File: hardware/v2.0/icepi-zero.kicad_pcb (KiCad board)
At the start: 4 copper layers, 65 x 30 mm, 193 parts, among them IC1 IS42S16160J-6BLI, IC2 LTC2256CUJ-12#PBF, J1 Conn_02x20_Counter_Clockwise, J2 GPDI_C_1.3, J3 USB_C_Receptacle_USB2.0_14P, J4 USB_C_Receptacle_USB2.0_14P, J5 USB_C_Receptacle_USB2.0_14P, J6 Micro_SD_Card_Det2, J7 RSP-122811-01, SW1 SW_Push, SW2 SW_Push, U1 ECP5U-25F-CABGA256, U10 TPD2EUSB30A, U11 LT1993CUD-2_PBF, U12 W25Q128JVS, U2 LTC3407AEDD-2_PBF, U3 TLV62569DBV, U4 LP5912-1.8DRV, U5 TPD2EUSB30A, U6 PCA9306DC1, U7 TPD2EUSB30A, U8 TPD2EUSB30A, U9 FT231XQ, Y1 SG-8018CG 50.000000MHz, Y2 SG-8018CG 50.000000MHz

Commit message: DRC almost pass
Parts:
- added C74: 1u, Capacitor_SMD:C_0402_1005Metric, B.Cu at (170.4, 107.3)
- added R5: 1k, Resistor_SMD:R_0402_1005Metric, B.Cu at (169.5, 107.3)
- moved R52 0.78 mm to (169.6, 105.0), turned to 0 degrees
- moved C64 0.17 mm to (168.3, 107.3)
- moved C69 0.07 mm to (171.3, 106.6)
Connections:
- R52 pad 1: /ADC/VOCM -> Net-(IC2-VCM)
- R52 pad 2: Net-(IC2-VCM) -> /ADC/VOCM
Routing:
- net /ADC/SENSE: track 23.9 -> 26.7 mm
- net +1V8: track 29.6 -> 31.1 mm
- net Net-(IC2-VCM): track 4.72 -> 3.60 mm
- net /ADC/VOCM: track 6.82 -> 7.79 mm
- net GND: vias 100 -> 98
- net /ADC/CLKOUT-: vias 0 -> 2

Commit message: ADC SPI SDO
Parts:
- moved LOGO1 0.28 mm to (177.0, 110.3)
- moved R1 0.14 mm to (161.2, 112.0)
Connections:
- IC2 pad 16: unconnected-(IC2-SDO-Pad16) -> /ADC/SDO
- U1 pad C12: unconnected-(U1J-PT56B/--PadC12) -> /ADC/~{CS}
- U1 pad D13: /ADC/~{CS} -> /ADC/SDO
- U1 pad E12: /ADC/SDI -> /ADC/SENSE
- U1 pad E13: /ADC/SENSE -> /ADC/SDI
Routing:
- net /ADC/SDO: track 0.00 -> 34.8 mm, vias 0 -> 3
- net /ADC/~{CS}: track 30.2 -> 28.7 mm
- net +3V3: track 126.2 -> 127.3 mm
- net /ADC/SDI: track 34.2 -> 35.2 mm
- net /ADC/SENSE: track 26.7 -> 25.9 mm
- net /ADC/SCK: track 30.9 -> 30.2 mm

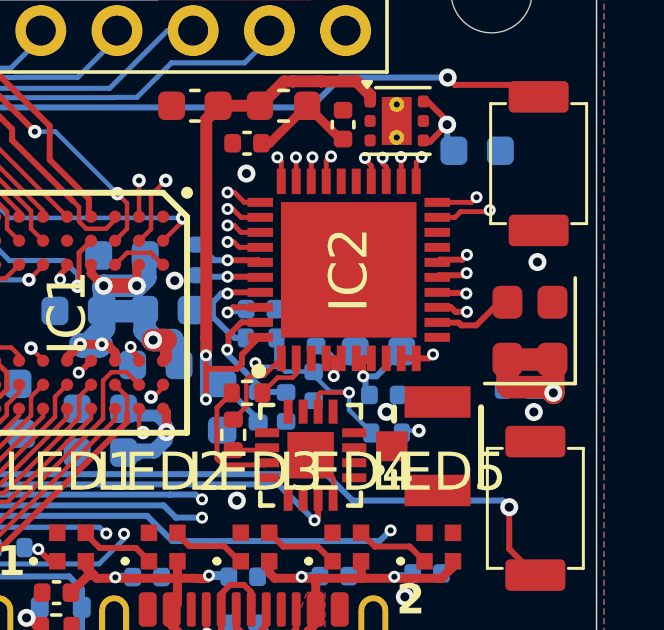
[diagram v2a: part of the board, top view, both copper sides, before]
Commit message: ADC SPI SDO pull up
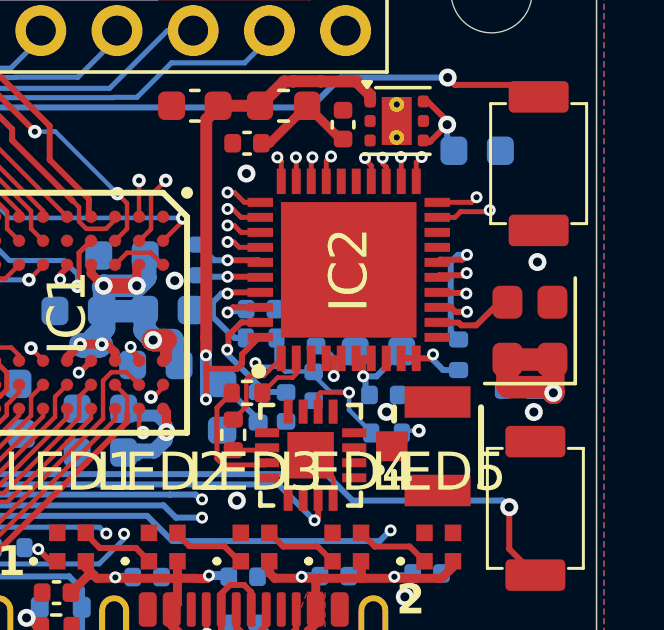
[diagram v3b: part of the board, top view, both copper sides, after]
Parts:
- added R56: 2k, Resistor_SMD:R_0402_1005Metric, B.Cu at (176.2, 105.6)
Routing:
- net /ADC/SDO: track 34.8 -> 38.1 mm
- net +1V8: track 31.1 -> 32.3 mm

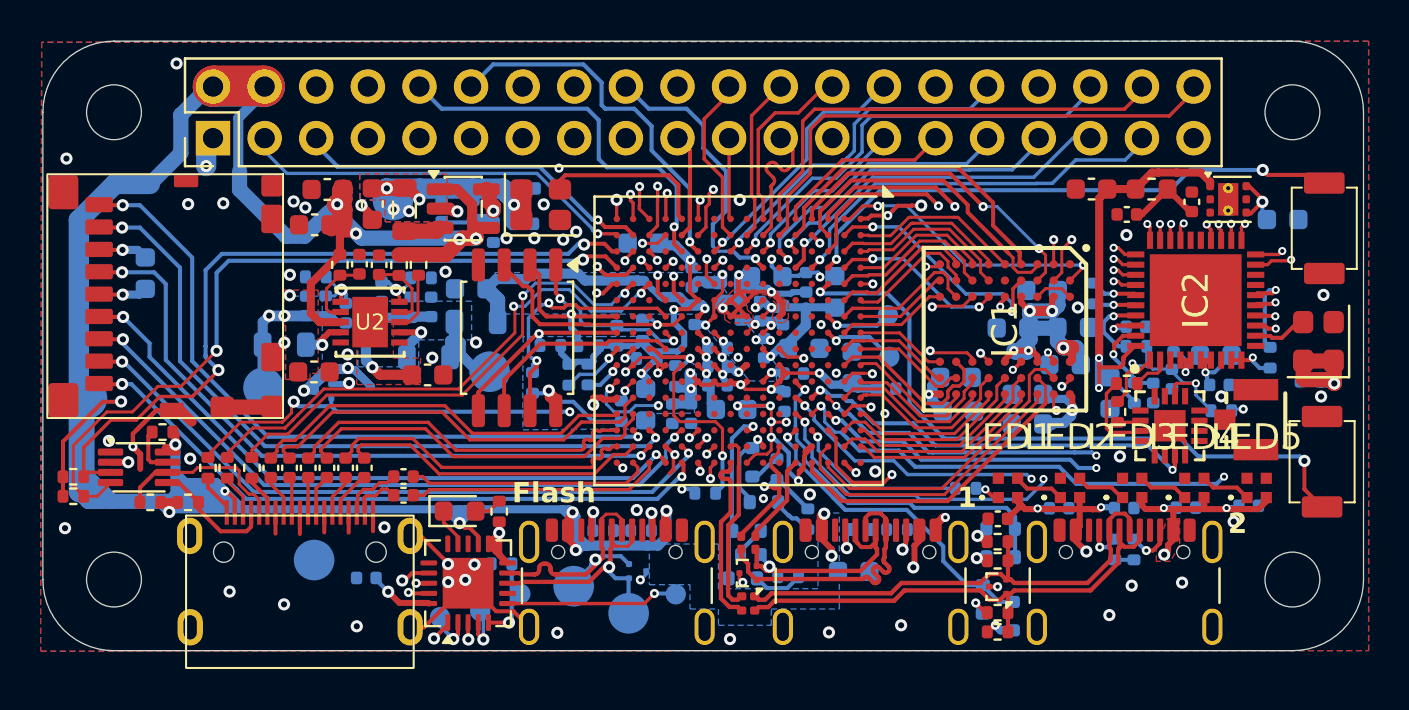
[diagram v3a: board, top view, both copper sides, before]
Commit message: HPD line protection
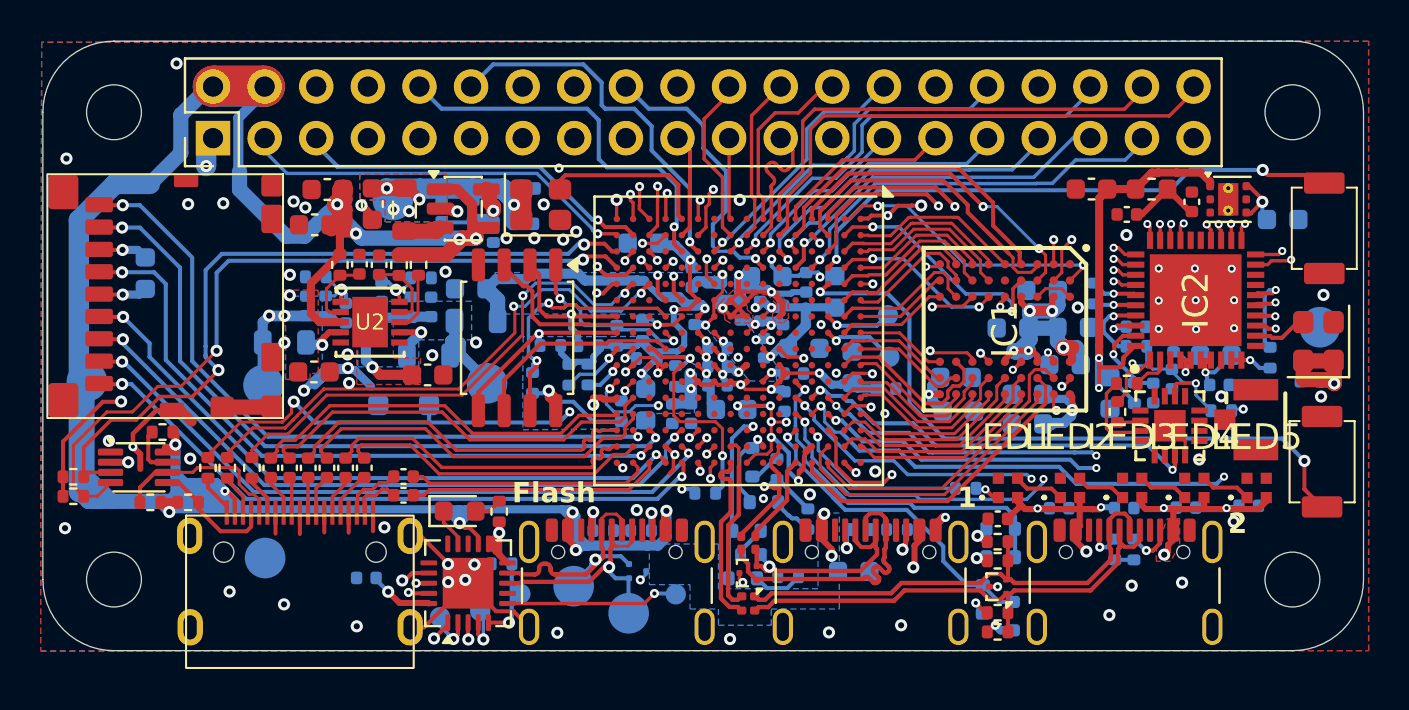
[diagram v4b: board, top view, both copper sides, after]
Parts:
- removed U5: TPD2EUSB30A, Package_TO_SOT_SMD:Texas_DRT-3
- added D1: 3V6, Diode_SMD:D_SOD-323_HandSoldering, B.Cu at (133.5, 107.9)
- Y2: value SG-8018CG 50.000000MHz -> SG-8018CG 25.000000MHz
- moved LOGO1 16.3 mm to (166.4, 97.9)
- moved TP1 6.33 mm to (178.6, 104.1)
- moved REF** 5.55 mm to (128.0, 110.7)
- moved REF** 4.41 mm to (120.4, 110.6)
- moved TP2 2.41 mm to (126.7, 115.4)
- moved TP3 0.84 mm to (117.9, 106.7)
- moved TP5 0.58 mm to (137.6, 106.8)
- moved TP6 0.13 mm to (126.6, 106.9)
- moved L1 0.11 mm to (127.6, 104.8)
- moved L2 0.08 mm to (134.7, 105.5)
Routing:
- net /GPDI/GPDI_HPD: track 26.9 -> 27.8 mm
- net +5V: track 218.9 -> 219.7 mm
- net /GPDI/GPDI_UTIL: track 27.2 -> 26.4 mm
- net GND: track 98.5 -> 97.7 mm, vias 98 -> 107
- net /ADC/CLKOUT+: track 27.0 -> 26.4 mm
- net /ADC/CLKOUT-: track 28.7 -> 28.0 mm
- net /ADC/D4_5-: track 34.0 -> 33.5 mm
- net /ADC/D4_5+: track 31.9 -> 31.4 mm
